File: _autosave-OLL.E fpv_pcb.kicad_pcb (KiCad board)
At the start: 6 copper layers, 47.6 x 41.5 mm, 130 parts, among them J1 Micro_SD_Card, J10 Conn_01x05_Pin, J2 RC, J8 reciver, J9 TYPE-C-31-M-12, M1 M1 front left, M2 M2 front right, M3 M3 rear right, M4 m4 rear left, Q1 2N7002, SW1 SW_SPST, SW2 SW_SPST, U1 MP2315GJ, U10 AON7410, U11 UCC27511ADBV, U12 AON7410, U13 BMP280, U14 STM32H753VITx, U15 USBLC6-2SC6, U3 MP2315GJ, U4 ICM-42688-P, U5 UCC27511ADBV, U6 ul_AON7410, U7 UCC27511ADBV, U8 AON7410, U9 UCC27511ADBV, Y2 8HMz

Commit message: update
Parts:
- removed C22, C44: 10uF/25v, Capacitor_SMD:C_0603_1608Metric
- added C13: 100nF, Capacitor_SMD:C_0603_1608Metric, B.Cu at (138.4, 107.3)
- added D9: BZX84C10, Package_TO_SOT_SMD:SOT-23, B.Cu at (135.4, 107.0)
- added Q2: SUD45P03-09, Package_TO_SOT_SMD:TO-252-2, B.Cu at (177.4, 88.7)
- added R33: 100k, Resistor_SMD:R_0603_1608Metric, F.Cu at (153.2, 88.4)
- added R34: 33k, Resistor_SMD:R_0603_1608Metric, F.Cu at (150.9, 93.4)
- added R7: 0 ohm, Resistor_SMD:R_0603_1608Metric, B.Cu at (179.8, 80.5)
- C14: value 10uF -> 100nF
- C15: moved to B.Cu
- C19: value 0.1µF -> 100nF
- C42, C43: value 12pF -> 15pF
- R1, R10: value 75k -> 100k
- REF**: value ESD-Logo_2.6mm_SilkScreen -> ESD-Logo_6.6x6mm_SilkScreen
- moved C14 10.5 mm to (153.4, 96.6), turned to 90 degrees
- moved U4 4.76 mm to (159.6, 100.9)
- moved REF** 3.96 mm to (156.9, 103.1)
- moved C15 1.93 mm to (143.2, 97.4)
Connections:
- BAT1 pad 1: +VBAT -> /VBAT_RAW
- C14 pad 1: +VBAT -> GND
- C14 pad 2: GND -> +VBAT
- R1 pad 1: Net-(R1-+) -> +VBAT
- R1 pad 2: GND -> Net-(R1--)
- R10 pad 1: Net-(R10-+) -> Net-(C13-+)
- U1 pad 1: Net-(R1-+) -> Net-(C8-+)
- U1 pad 6: +5V_FC -> Net-(R33-+)
- U14 pad 13: Net-(C43-+) -> Net-(R7--)
- U3 pad 1: Net-(R10-+) -> Net-(C19-+)
- U3 pad 6: +VBAT -> Net-(R1--)
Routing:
- net GND: track 330.6 -> 396.4 mm, vias 33 -> 87
- net Net-(C13-+): track 0.00 -> 64.8 mm, vias 0 -> 4
- net +VBAT: track 172.5 -> 112.8 mm, vias 9 -> 41
- net /VBAT_RAW: track 0.00 -> 56.2 mm, vias 0 -> 2
- net +3V3_FC: track 165.0 -> 201.6 mm, vias 14 -> 15
- net Net-(C43-+): track 12.8 -> 39.1 mm, vias 2 -> 3
- net Net-(R1--): track 0.00 -> 24.4 mm, vias 0 -> 3
- net Net-(R7--): track 0.00 -> 23.8 mm, vias 0 -> 2
- net C1_D0: track 66.3 -> 84.4 mm
- net Net-(R33-+): track 0.00 -> 8.58 mm, vias 0 -> 2
- net SPI1_SDO: track 3.95 -> 10.7 mm
- net Net-(C8-+): track 13.7 -> 20.2 mm
- net SPI1_SDI: track 3.82 -> 10.3 mm
- net +5V_FC: track 180.4 -> 186.7 mm, vias 15 -> 16
- net GYRO_CS: track 8.67 -> 14.8 mm
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- added copper zone on B.Cu, net +VBAT
- added copper zone on In2.Cu, net GND
- added copper zone on In3.Cu, net GND
- removed copper zone on F.Cu, net +3V3_FC

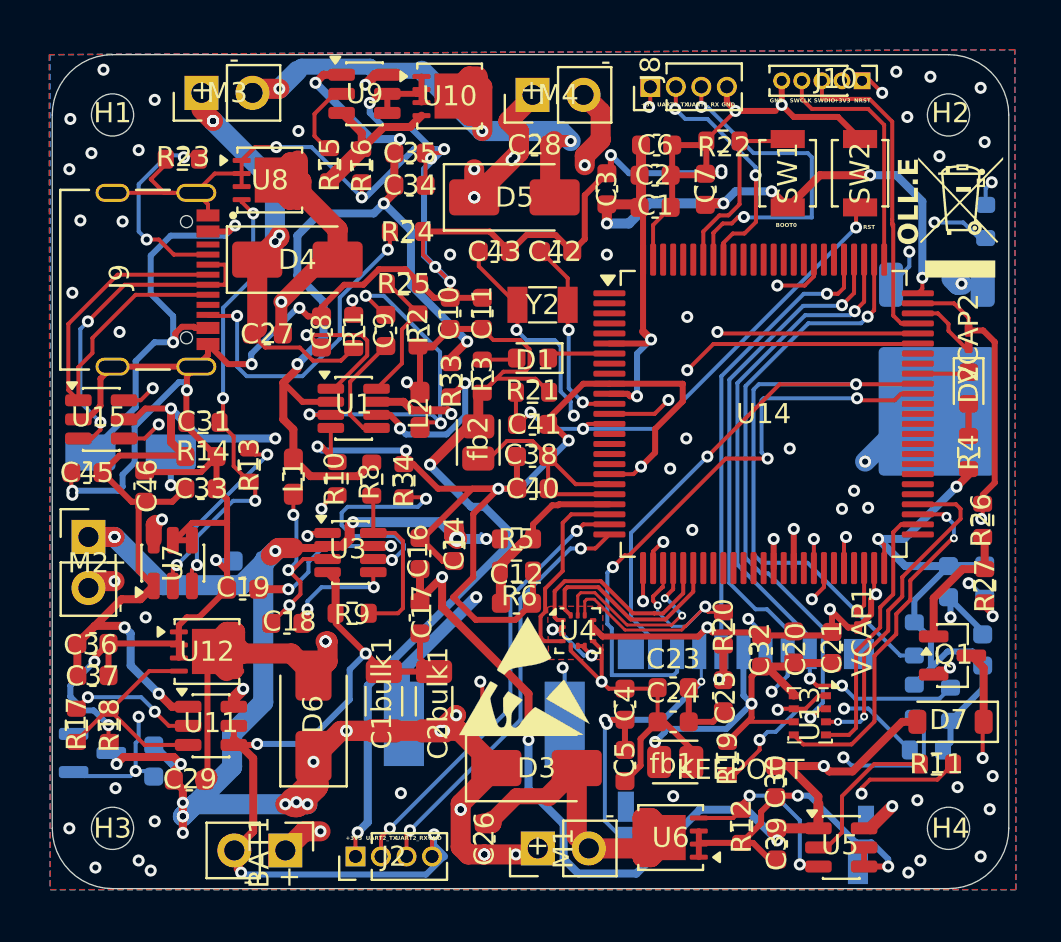
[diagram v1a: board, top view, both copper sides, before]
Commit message: update poller capictor 220uF/25
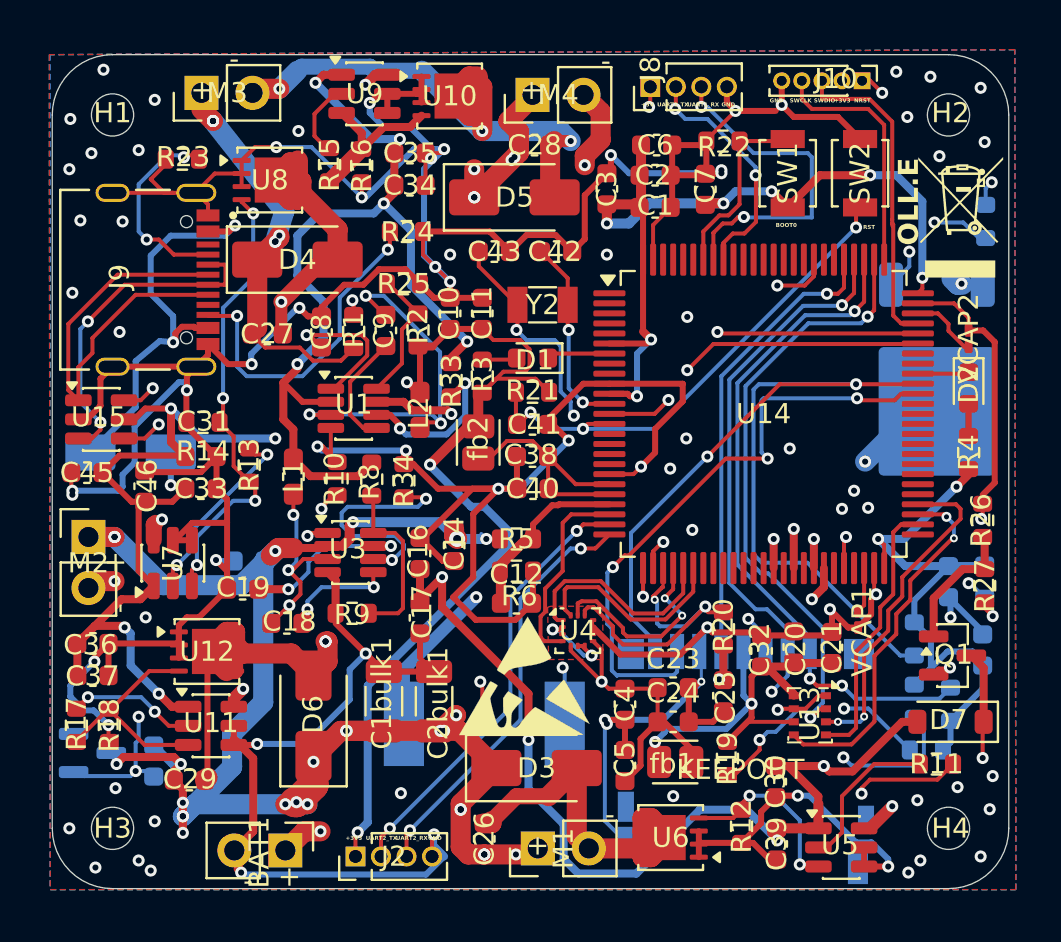
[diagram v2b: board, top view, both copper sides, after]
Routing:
- net SPI1_SCK: track 10.1 -> 10.8 mm
